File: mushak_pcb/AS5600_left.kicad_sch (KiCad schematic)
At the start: 7 parts, among them IC1 AS5600-ASOT

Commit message: Add footprints
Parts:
- C22, C23: footprint (none) -> Capacitor_SMD:C_0805_2012Metric
- IC1: footprint SOIC127P600X175-8N -> AS5600-ASOT:SOIC127P600X175-8N
- TP15, TP16: footprint (none) -> TestPoint:TestPoint_Pad_2.5x2.5mm
- TP17, TP18: footprint (none) -> TestPoint:TestPoint_Keystone_5019_Minature
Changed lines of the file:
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@@
       (effects (font (size 1.27 1.27)) (justify left))
     )
-    (property "Footprint" "" (id 2) (at 137.16 85.09 0)
+    (property "Footprint" "TestPoint:TestPoint_Pad_2.5x2.5mm" (id 2) (at 137.16 85.09 0)
       (effects (font (size 1.27 1.27)) hide)
     )
@@
     (property "Reference" "IC1" (id 0) (at 154.94 85.09 0))
     (property "Value" "AS5600-ASOT" (id 1) (at 154.94 87.63 0))
-    (property "Footprint" "SOIC127P600X175-8N" (id 2) (at 139.7 92.71 0)
+    (property "Footprint" "AS5600-ASOT:SOIC127P600X175-8N" (id 2) (at 139.7 92.71 0)
       (effects (font (size 1.27 1.27)) (justify left bottom) hide)
     )
@@
       (effects (font (size 1 1)) (justify left))
     )
-    (property "Footprint" "" (id 2) (at 176.53 102.87 0)
+    (property "Footprint" "TestPoint:TestPoint_Keystone_5019_Minature" (id 2) (at 176.53 102.87 0)
       (effects (font (size 1.27 1.27)) hide)
     )
@@
       (effects (font (size 1.27 1.27)) (justify left))
     )
-    (property "Footprint" "" (id 2) (at 136.8552 107.95 0)
+    (property "Footprint" "Capacitor_SMD:C_0805_2012Metric" (id 2) (at 136.8552 107.95 0)
       (effects (font (size 1.27 1.27)) hide)
     )
@@
       (effects (font (size 1.27 1.27)) (justify right))
     )
-    (property "Footprint" "" (id 2) (at 119.38 107.95 0)
+    (property "Footprint" "TestPoint:TestPoint_Pad_2.5x2.5mm" (id 2) (at 119.38 107.95 0)
       (effects (font (size 1.27 1.27)) hide)
     )
@@
       (effects (font (size 1 1)) (justify left))
     )
-    (property "Footprint" "" (id 2) (at 176.53 100.33 0)
+    (property "Footprint" "TestPoint:TestPoint_Keystone_5019_Minature" (id 2) (at 176.53 100.33 0)
       (effects (font (size 1.27 1.27)) hide)
     )
@@
       (effects (font (size 1.27 1.27)) (justify left))
     )
-    (property "Footprint" "" (id 2) (at 130.5052 107.95 0)
+    (property "Footprint" "Capacitor_SMD:C_0805_2012Metric" (id 2) (at 130.5052 107.95 0)
       (effects (font (size 1.27 1.27)) hide)
     )

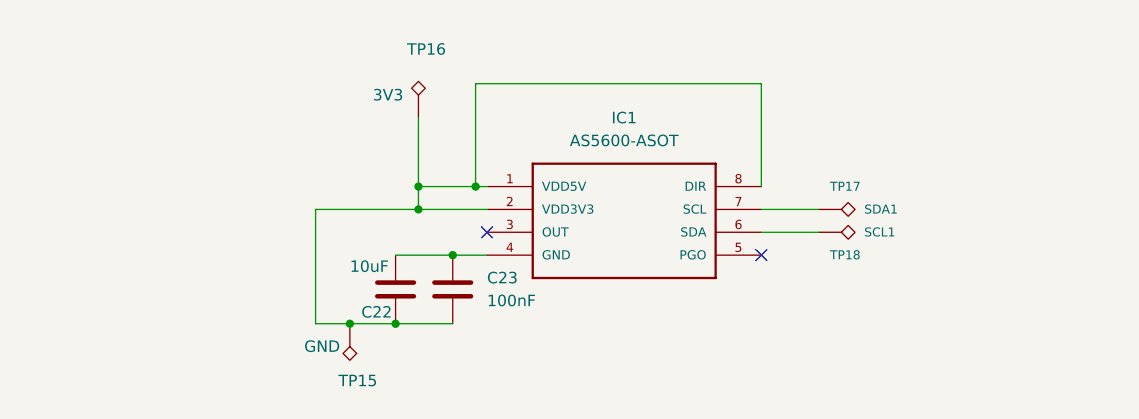
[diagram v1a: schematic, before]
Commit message: Update Schematics and footprints for sensors
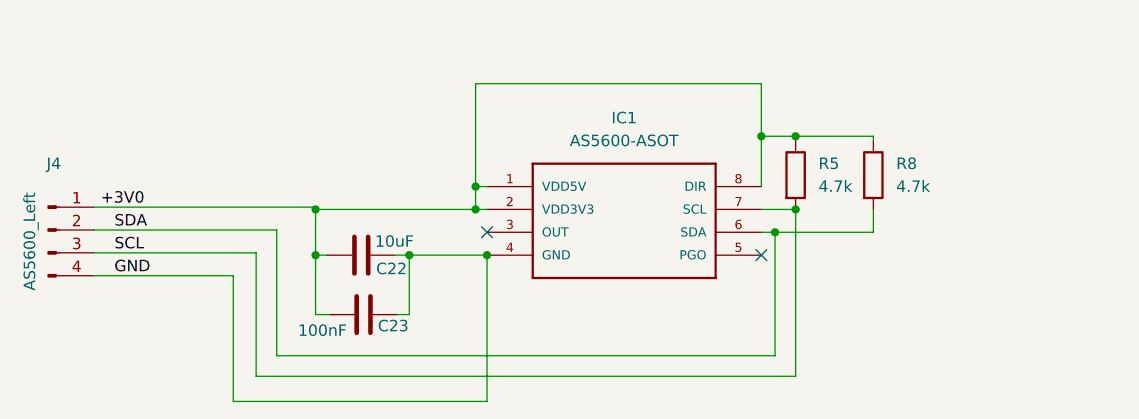
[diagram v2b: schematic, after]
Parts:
- removed TP15: GND, TestPoint:TestPoint_Pad_2.5x2.5mm, symbol Connector:TestPoint_Alt
- removed TP16: 3V3, TestPoint:TestPoint_Pad_2.5x2.5mm, symbol Connector:TestPoint_Alt
- removed TP17: SDA1, TestPoint:TestPoint_Keystone_5019_Minature, symbol Connector:TestPoint_Alt
- removed TP18: SCL1, TestPoint:TestPoint_Keystone_5019_Minature, symbol Connector:TestPoint_Alt
- added J4: AS5600_Left, mushak_mount_footprint:STAND_SLAVE_04, symbol Connector:Conn_01x04_Male
- added R5, R8: 4.7k, Resistor_SMD:R_0402_1005Metric, symbol Device:R
- C22, C23: footprint Capacitor_SMD:C_0805_2012Metric -> Capacitor_SMD:C_0402_1005Metric
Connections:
- net +3V0: now reaches IC1.1 (VDD5V), IC1.2 (VDD3V3), IC1.8 (DIR)
- net +3V0: now also C22.1, C23.1, J4.1 (Pin_1), R5.1, R8.1; no longer C22.2, C23.2
- net SDA: now reaches IC1.6 (SDA)
- net SDA: now also J4.2 (Pin_2), R8.2
- net SCL: now reaches IC1.7 (SCL)
- net SCL: now also J4.3 (Pin_3), R5.2
- new net GND: C22.2, C23.2, IC1.4 (GND), J4.4 (Pin_4)
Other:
- moved on the sheet: C22, C23

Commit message: changed footprints of capacitors and resistors
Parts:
- R5, R8: footprint Resistor_SMD:R_0402_1005Metric -> Resistor_SMD:R_0201_0603Metric
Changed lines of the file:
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@@
       (effects (font (size 1.27 1.27)) (justify left))
     )
-    (property "Footprint" "Resistor_SMD:R_0402_1005Metric" (id 2) (at 172.212 91.44 90)
+    (property "Footprint" "Resistor_SMD:R_0201_0603Metric" (id 2) (at 172.212 91.44 90)
       (effects (font (size 1.27 1.27)) hide)
     )
@@
       (effects (font (size 1.27 1.27)) (justify left))
     )
-    (property "Footprint" "Resistor_SMD:R_0402_1005Metric" (id 2) (at 180.848 91.44 90)
+    (property "Footprint" "Resistor_SMD:R_0201_0603Metric" (id 2) (at 180.848 91.44 90)
       (effects (font (size 1.27 1.27)) hide)
     )

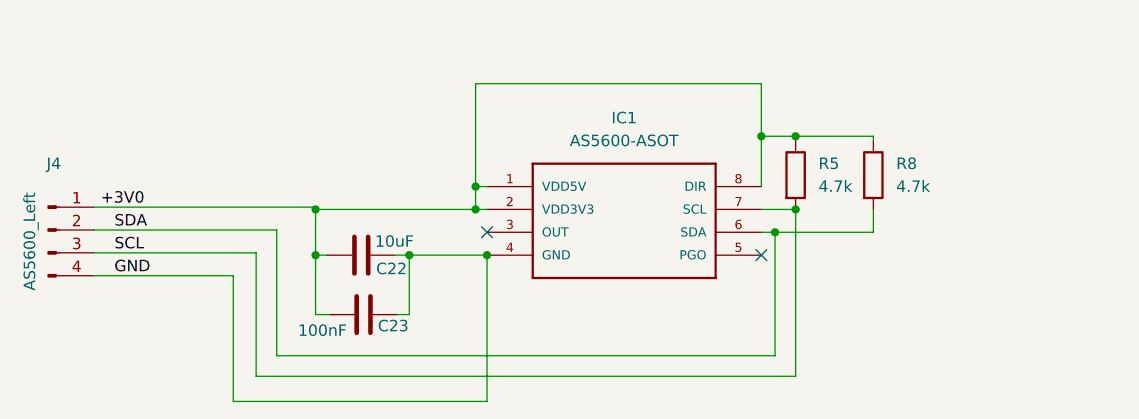
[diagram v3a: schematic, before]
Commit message: made draft pcb footprint placement
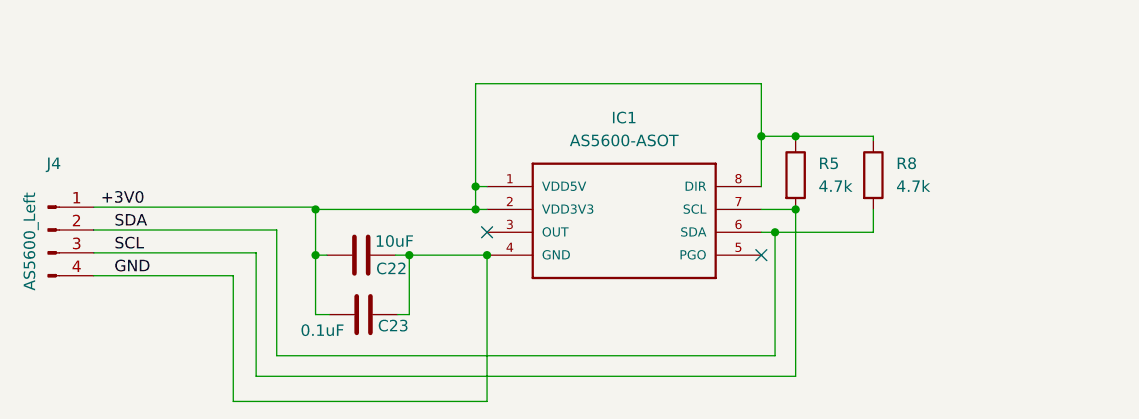
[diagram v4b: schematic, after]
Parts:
- C23: value 100nF -> 0.1uF
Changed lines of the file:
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@@
     (in_bom yes) (on_board yes)
     (property "Reference" "C23" (id 0) (at 129.286 108.204 90))
-    (property "Value" "100nF" (id 1) (at 121.412 108.712 90))
+    (property "Value" "0.1uF" (id 1) (at 121.412 108.712 90))
     (property "Footprint" "Capacitor_SMD:C_0402_1005Metric" (id 2) (at 129.794 105.9688 0)
       (effects (font (size 1.27 1.27)) hide)

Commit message: updated footprint for motors
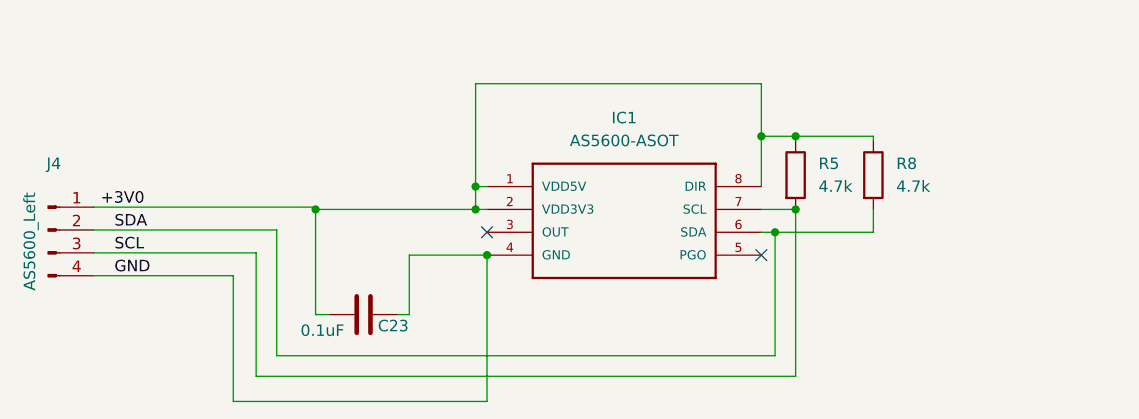
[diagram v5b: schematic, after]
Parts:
- removed C22: 10uF, Capacitor_SMD:C_0402_1005Metric, symbol Device:C
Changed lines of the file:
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@@
   (junction (at 173.99 87.122) (diameter 0) (color 0 0 0 0)
   )
-  (junction (at 131.064 100.33) (diameter 0) (color 0 0 0 0)
-  )
   (junction (at 173.99 95.25) (diameter 0) (color 0 0 0 0)
-  )
-  (junction (at 120.65 100.33) (diameter 0) (color 0 0 0 0)
   )
   (junction (at 138.43 95.25) (diameter 0) (color 0 0 0 0)
@@
     (stroke (width 0) (type default) (color 0 0 0 0))
   )
-  (wire (pts (xy 120.65 106.934) (xy 120.65 100.33))
+  (wire (pts (xy 120.65 95.25) (xy 120.65 106.934))
     (stroke (width 0) (type default) (color 0 0 0 0))
   )
@@
     (stroke (width 0) (type default) (color 0 0 0 0))
   )
-  (wire (pts (xy 129.54 100.33) (xy 131.064 100.33))
-    (stroke (width 0) (type default) (color 0 0 0 0))
-  )
-  (wire (pts (xy 120.65 100.33) (xy 121.92 100.33))
-    (stroke (width 0) (type default) (color 0 0 0 0))
-  )
   (wire (pts (xy 171.704 97.79) (xy 170.18 97.79))
     (stroke (width 0) (type default) (color 0 0 0 0))
   )
   (wire (pts (xy 173.99 87.63) (xy 173.99 87.122))
-    (stroke (width 0) (type default) (color 0 0 0 0))
-  )
-  (wire (pts (xy 120.65 95.25) (xy 120.65 100.33))
     (stroke (width 0) (type default) (color 0 0 0 0))
   )
@@
       (effects (font (size 1.27 1.27)) hide)
     )
-    (pin "1")
-    (pin "2")
-  )
-  (symbol (lib_id "Device:C") (at 125.73 100.33 90) (unit 1)
-    (in_bom yes) (on_board yes)
-    (property "Reference" "C22" (id 0) (at 130.81 101.854 90)
-      (effects (font (size 1.27 1.27)) (justify left))
-    )
-    (property "Value" "10uF" (id 1) (at 131.572 98.806 90)
-      (effects (font (size 1.27 1.27)) (justify left))
-    )
-    (property "Footprint" "Capacitor_SMD:C_0402_1005Metric" (id 2) (at 129.54 99.3648 0)
-      (effects (font (size 1.27 1.27)) hide)
-    )
-    (property "Datasheet" "~" (id 3) (at 125.73 100.33 0)
-      (effects (font (size 1.27 1.27)) hide)
-    )

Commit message: corrected encoder and motor driver schematics
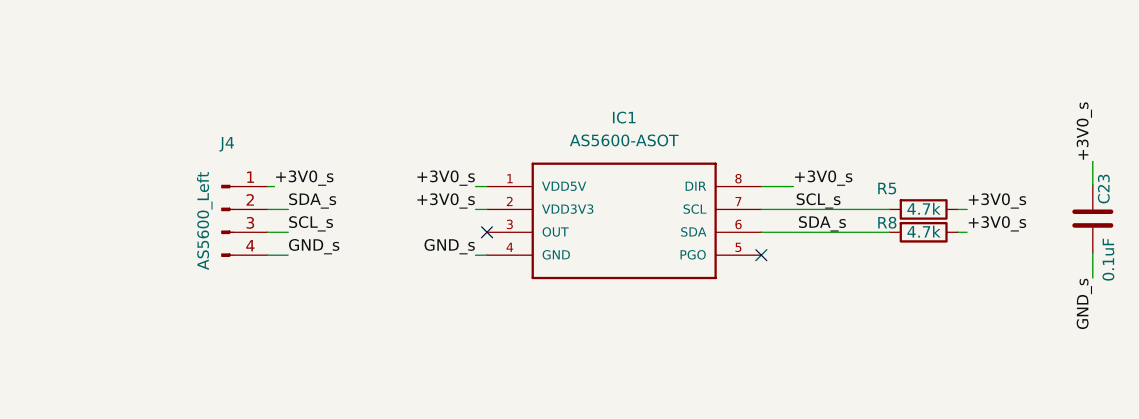
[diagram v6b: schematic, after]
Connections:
- net +3V0 renamed +3V0_s
- net +3V0_s: now also C23.2; no longer C23.1
- net GND renamed GND_s
- net GND_s: now also C23.1; no longer C23.2
- net SCL renamed SCL_s
- net SCL_s: now also R8.2; no longer R5.2
- net SDA renamed SDA_s
- net SDA_s: now also R5.2; no longer R8.2
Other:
- moved on the sheet: C23, J4, R5, R8

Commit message: changed footprint of passive components
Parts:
- R5, R8: footprint Resistor_SMD:R_0201_0603Metric -> Resistor_SMD:R_0402_1005Metric
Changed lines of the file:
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@@
     (property "Reference" "R5" (id 0) (at 184.15 92.964 90))
     (property "Value" "4.7k" (id 1) (at 188.214 97.79 90))
-    (property "Footprint" "Resistor_SMD:R_0201_0603Metric" (id 2) (at 188.214 96.012 90)
+    (property "Footprint" "Resistor_SMD:R_0402_1005Metric" (id 2) (at 188.214 96.012 90)
       (effects (font (size 1.27 1.27)) hide)
     )
@@
     (property "Reference" "R8" (id 0) (at 184.15 96.774 90))
     (property "Value" "4.7k" (id 1) (at 188.214 95.25 90))
-    (property "Footprint" "Resistor_SMD:R_0201_0603Metric" (id 2) (at 188.214 93.472 90)
+    (property "Footprint" "Resistor_SMD:R_0402_1005Metric" (id 2) (at 188.214 93.472 90)
       (effects (font (size 1.27 1.27)) hide)
     )

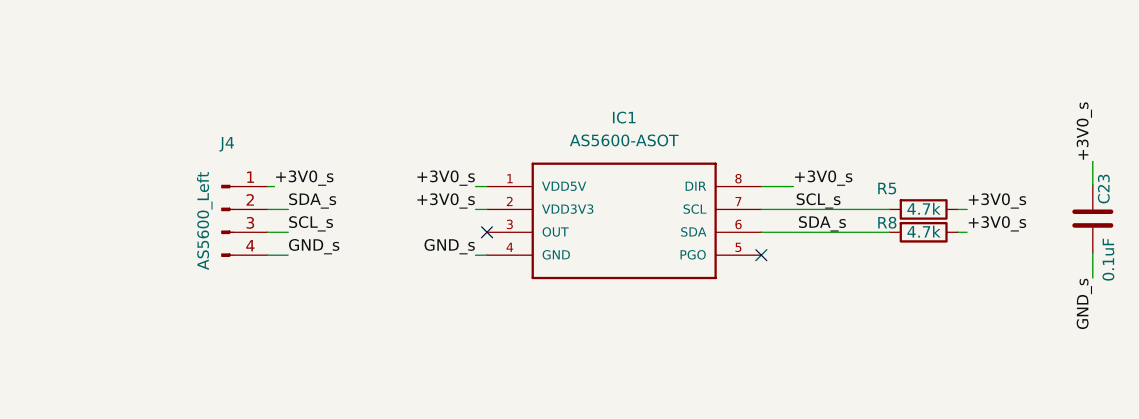
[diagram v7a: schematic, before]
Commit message: changed oscilattor placement
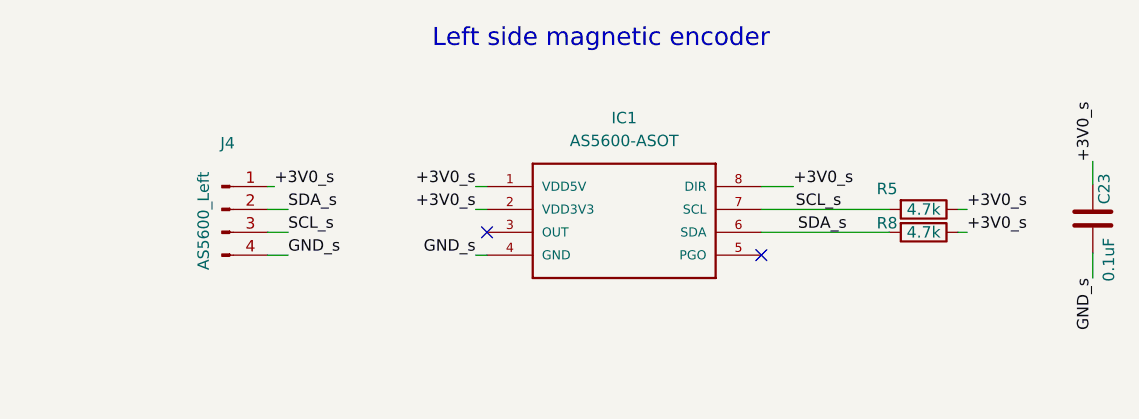
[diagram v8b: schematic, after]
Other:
- note added: "Left side magnetic encoder"
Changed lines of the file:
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@@
     (stroke (width 0) (type default) (color 0 0 0 0))
+  )
+  (text "Left side magnetic encoder" (at 133.604 77.47 0)
+    (effects (font (size 2 2)) (justify left bottom))
   )
   (label "GND_s" (at 207.01 102.87 270)
